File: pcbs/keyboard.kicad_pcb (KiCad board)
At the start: 2 copper layers, 380.3 x 157 mm, 222 parts, among them J1 MJ-4PP-9, J2 MJ-4PP-9, SW1 SW_PUSH, SW2 SW_PUSH, SW3 RotaryEncoder_Switch, U1 ProMicro, U3 ProMicro

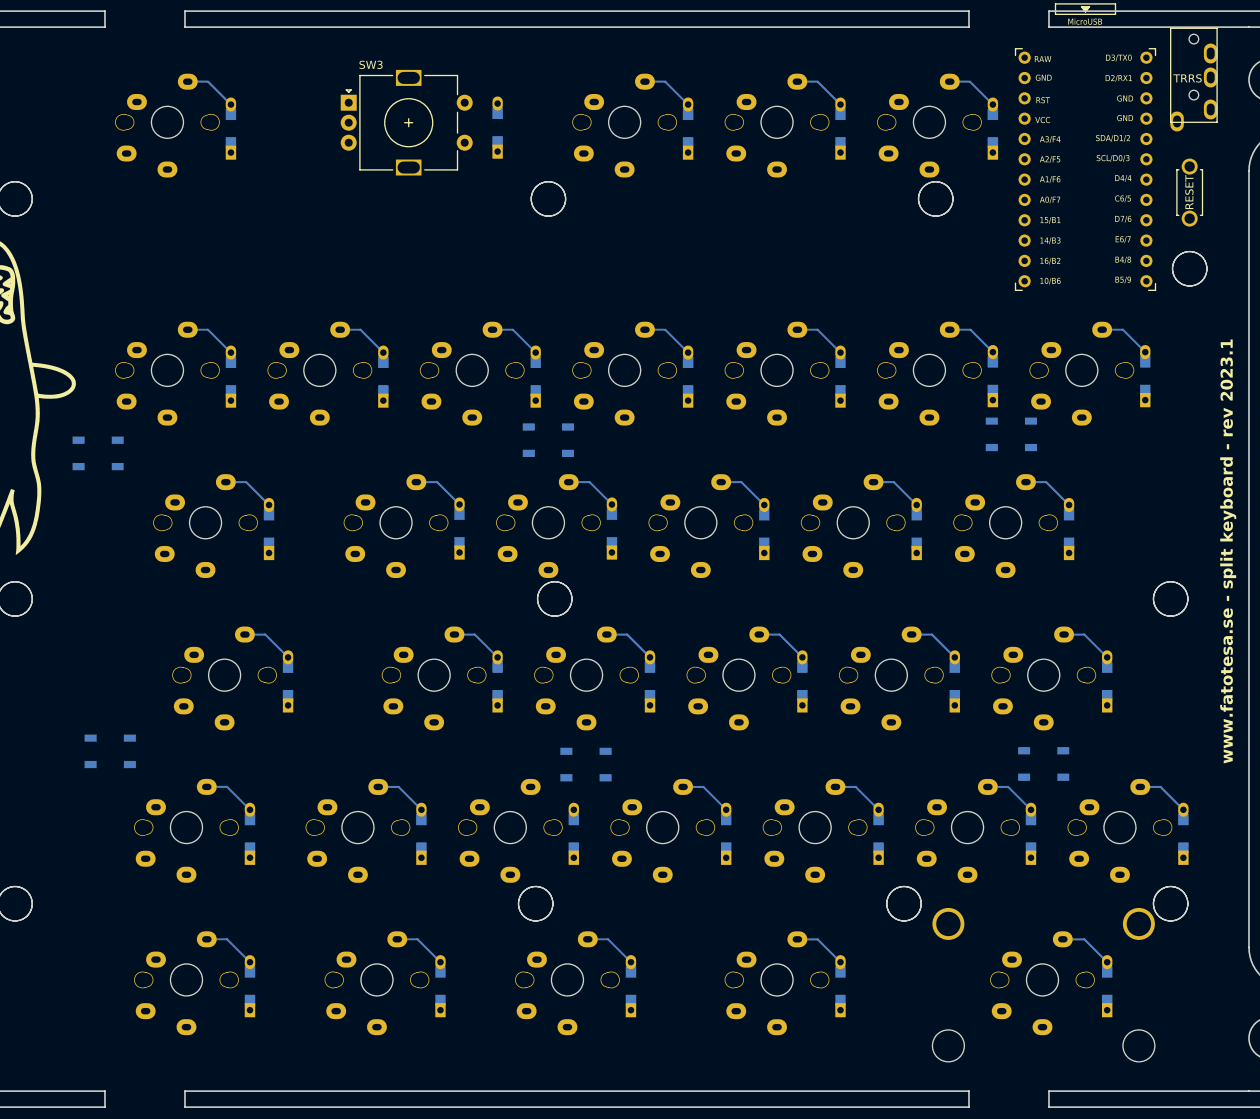
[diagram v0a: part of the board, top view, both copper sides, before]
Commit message: Wired up the left side.
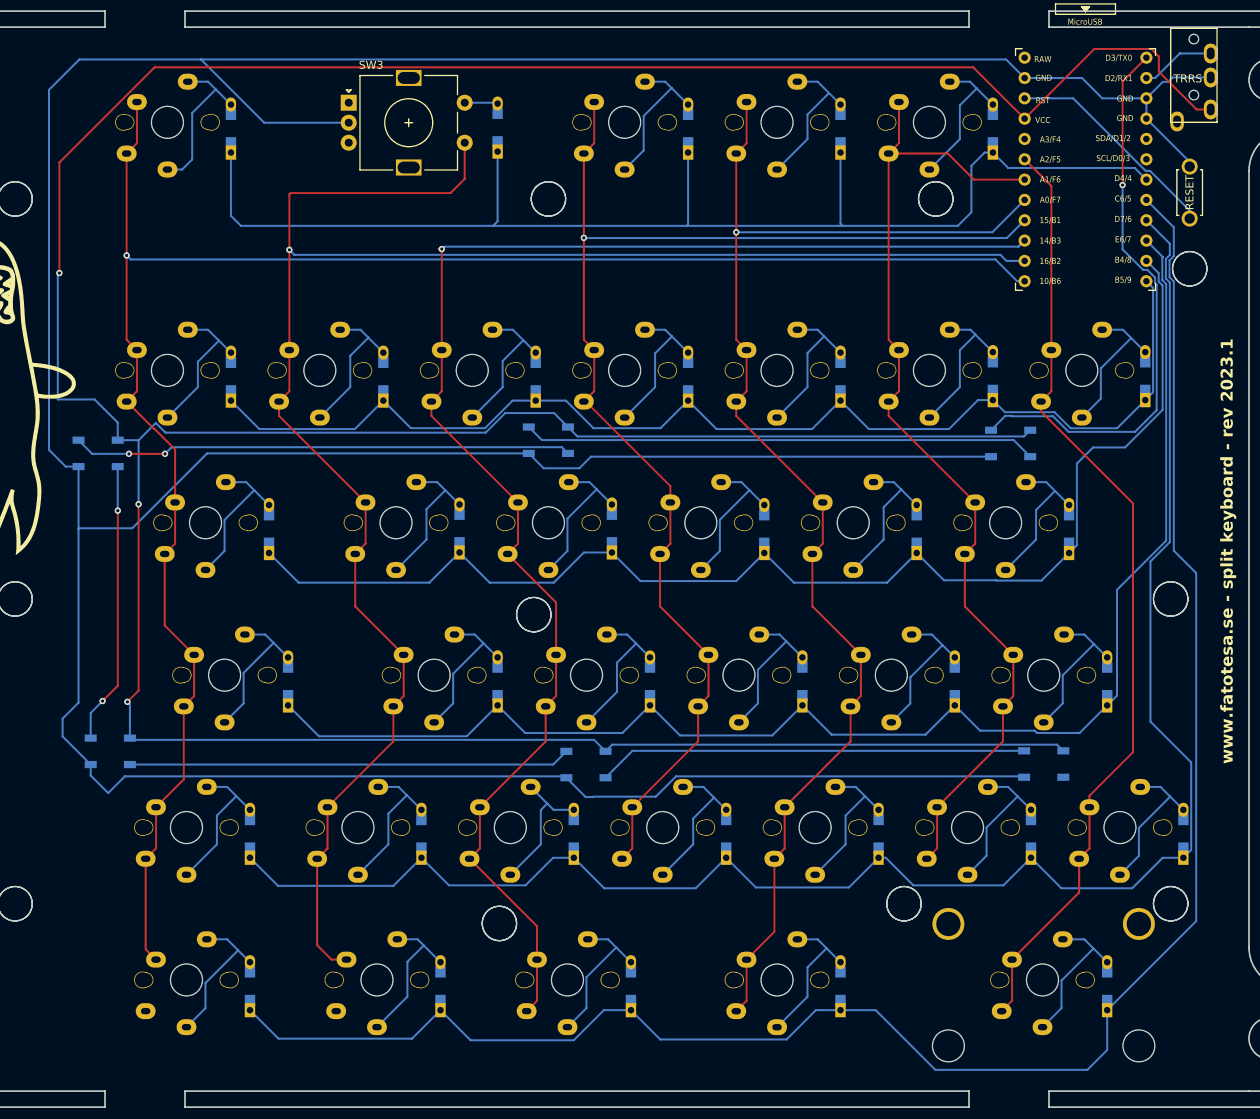
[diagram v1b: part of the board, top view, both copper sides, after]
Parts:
- moved ? 5.17 mm to (154.2, 237.4) (x2)
- moved ? 3.27 mm to (158.5, 198.8) (x2)
- moved LED5 1.14 mm to (218.1, 177.4)
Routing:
- net GND: track 0.00 -> 512.8 mm
- net VCC: track 0.00 -> 473.9 mm, vias 0 -> 3
- net row6: track 0.00 -> 234.3 mm
- net col1: track 0.00 -> 231.6 mm, vias 0 -> 1
- net col0: track 0.00 -> 230.0 mm, vias 0 -> 1
- net row5: track 0.00 -> 219.5 mm
- net col2: track 0.00 -> 185.3 mm, vias 0 -> 1
- net row4: track 0.00 -> 179.7 mm
- net col4: track 0.00 -> 167.0 mm, vias 0 -> 1
- net col3: track 0.00 -> 164.4 mm, vias 0 -> 1
- net row3: track 0.00 -> 159.6 mm
- net row0: track 0.00 -> 159.5 mm
- net row2: track 0.00 -> 147.4 mm
- net col5: track 0.00 -> 126.6 mm
- net col6: track 0.00 -> 120.0 mm
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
